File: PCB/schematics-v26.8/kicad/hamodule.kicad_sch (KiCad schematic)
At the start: 191 parts, among them J1 GND|5V, J10 Tx|Rx, J11 Sda|Scl, J12 3|9, J13 13|12, J14 3.3v|GND|7|15, J15 2604-1104, J16 2604-1104, J17 TestPoint, J19 TestPoint, J2 2604-1102, J3 USB_C_Receptacle_USB2.0, J4 GND|3.3V, J5 Conn_01x02_Pin, J6 2604-1104, J7 2604-1104, J8 5v|GND|Do, J9 Screen, K1 AQG22205, K2 AQG22205, K3 AQG22205, K4 AQG22205, K5 AQG22205, K6 AQG22205, K7 AQG22205, K8 AQG22205, SW1 USB | PS, SW2 Reset, SW3 Boot, U1 LD1117AV33, U10 SN74LV1T34DBV, U11 ULN2803A, U12 TCAL6416, U14 74AHC1G04, U2 USBLC6-2SC6, U3 ESP32-S3-WROOM-2, U4 LDA210, U5 LDA210, U6 LDA210, U7 LDA210, U8 SHT4x, U9 SN74LVCH8T245

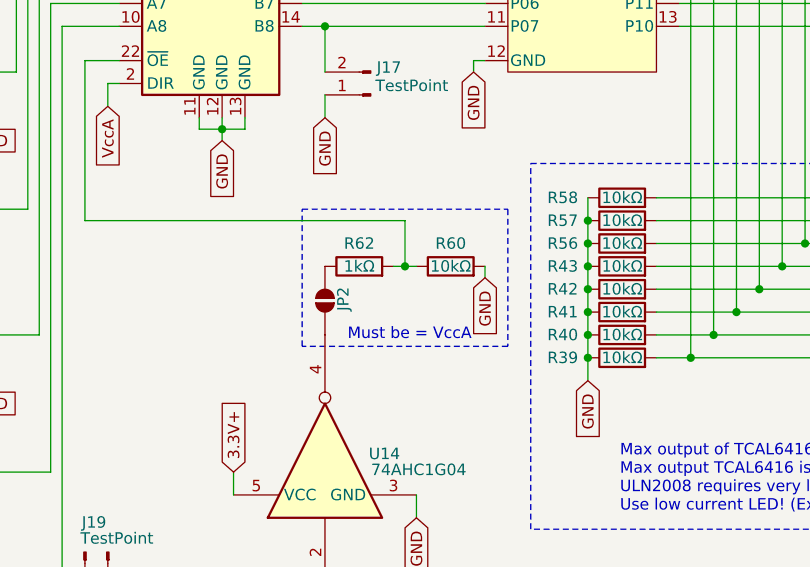
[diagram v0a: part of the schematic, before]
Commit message: areas were not properly filled in PCB
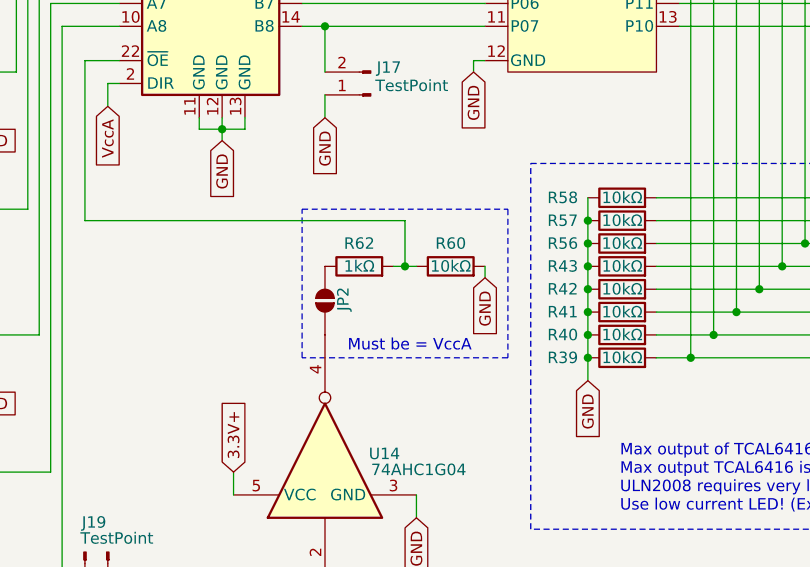
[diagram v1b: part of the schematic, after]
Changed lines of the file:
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@@
 	(rectangle
 		(start 246.38 127)
-		(end 269.24 142.24)
+		(end 269.24 143.51)
 		(stroke
 			(width 0)
@@
 	(text "Must be = VccA"
 		(exclude_from_sim no)
-		(at 258.318 140.97 0)
+		(at 258.318 142.24 0)
 		(effects
 			(font

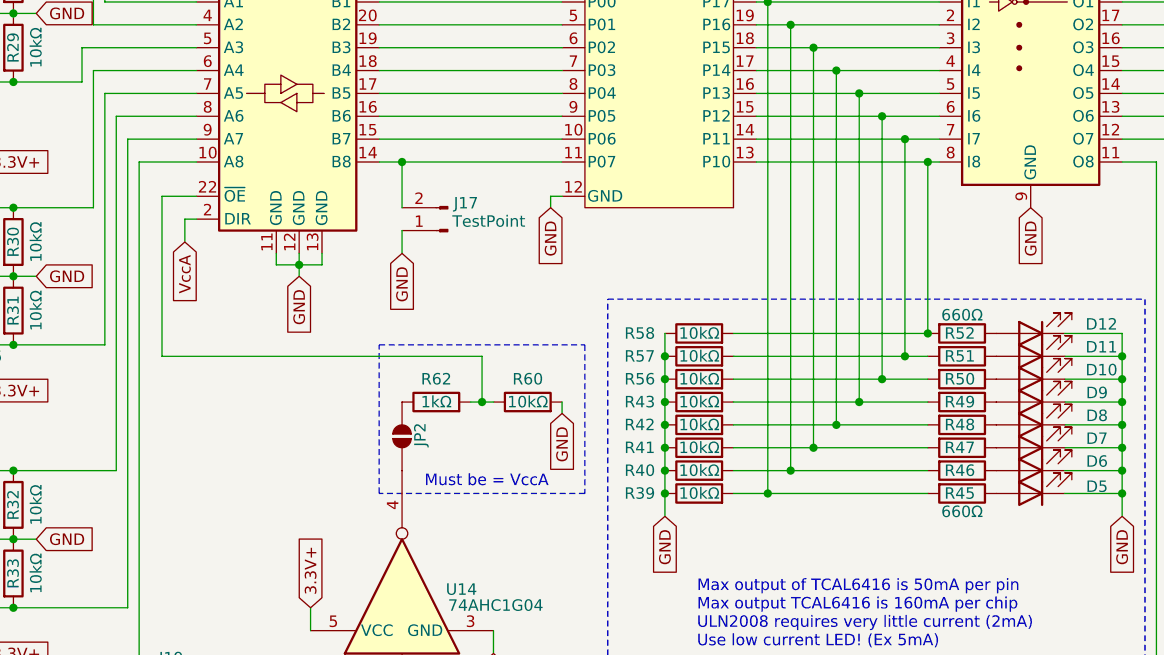
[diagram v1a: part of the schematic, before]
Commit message: Adding Test point for TCAL to ULN. Small astetic change in the schematic: Moving the voltage divider resistors after the NOT gate
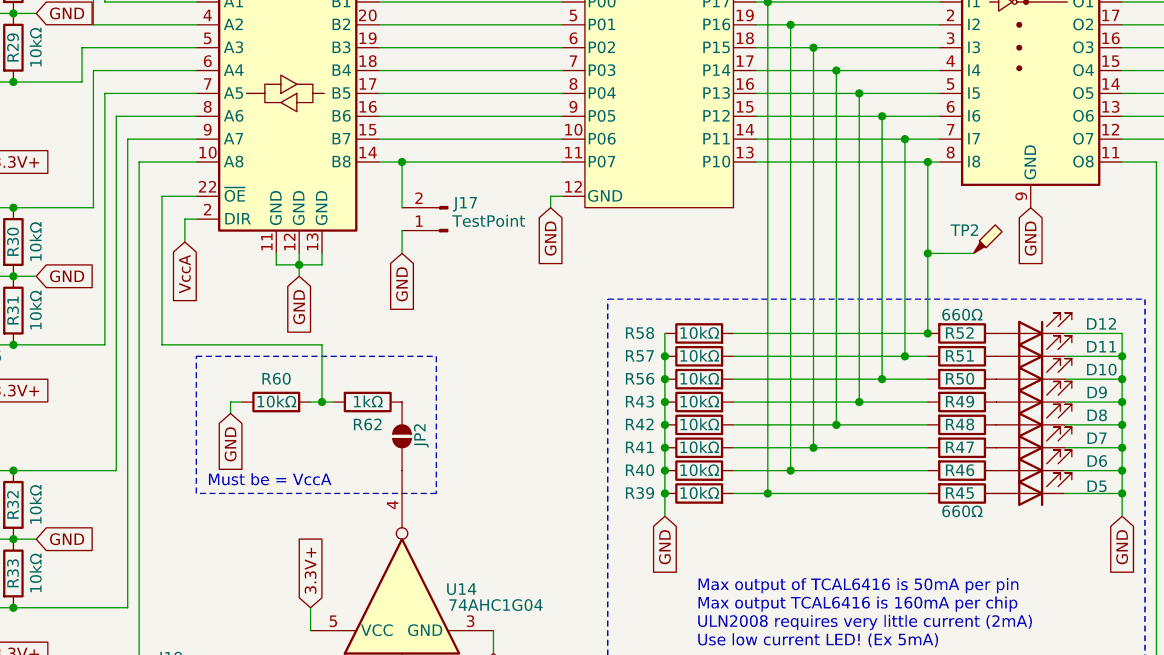
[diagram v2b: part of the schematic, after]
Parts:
- added TP2: GND, TestPoint:TestPoint_THTPad_1.0x1.0mm_Drill0.5mm, symbol Connector:TestPoint_Probe
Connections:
- net GND: now also R60.1; no longer R60.2
- net at R62.2, U9.22 (~{OE}): now also R60.2; no longer R60.1
- net at R52.2, R58.2, U11.8 (I8)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: now also TP2.1
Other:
- moved on the sheet: R60, R62
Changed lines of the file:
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@@
 	)
 	(rectangle
-		(start 246.38 127)
-		(end 269.24 143.51)
+		(start 226.06 128.27)
+		(end 252.73 143.51)
 		(stroke
 			(width 0)
@@
 	(text "Must be = VccA"
 		(exclude_from_sim no)
-		(at 258.318 142.24 0)
+		(at 234.188 142.24 0)
 		(effects
 			(font
@@
 	)
 	(junction
-		(at 257.81 133.35)
-		(diameter 0)
-		(color 0 0 0 0)
-	)
-	(junction
 		(at 95.25 77.47)
 		(diameter 0)
@@
 	)
 	(junction
+		(at 240.03 133.35)
+		(diameter 0)
+		(color 0 0 0 0)
+	)
+	(junction
 		(at 207.01 215.9)
 		(diameter 0)
@@
 	)
 	(junction
+		(at 307.34 116.84)
+		(diameter 0)
+		(color 0 0 0 0)
+	)
+	(junction
 		(at 278.13 138.43)
 		(diameter 0)
@@
 	(wire
 		(pts
+			(xy 238.76 133.35) (xy 240.03 133.35)
+		)
+		(stroke
+			(width 0)
+			(type default)
+		)
+	)
+	(wire
+		(pts
 			(xy 292.1 215.9) (xy 295.91 215.9)
 		)
@@
 	(wire
 		(pts
+			(xy 240.03 133.35) (xy 241.3 133.35)
+		)
+		(stroke
+			(width 0)
+			(type default)
+		)
+	)
+	(wire
+		(pts
 			(xy 63.5 133.35) (xy 63.5 130.81)
 		)
@@
 	(wire
 		(pts
-			(xy 257.81 133.35) (xy 259.08 133.35)
-		)
-		(stroke
-			(width 0)
-			(type default)
-		)
-	)
-	(wire
-		(pts
 			(xy 328.93 93.98) (xy 339.09 93.98)
 		)
@@
 	(wire
 		(pts
+			(xy 307.34 116.84) (xy 312.42 116.84)
+		)
+		(stroke
+			(width 0)
+			(type default)
+		)
+	)
+	(wire
+		(pts
 			(xy 382.27 113.03) (xy 368.3 113.03)
 		)
@@
 	(wire
 		(pts
+			(xy 229.87 134.62) (xy 229.87 133.35)
+		)
+		(stroke
+			(width 0)
+			(type default)
+		)
+	)
+	(wire
+		(pts
 			(xy 265.43 73.66) (xy 266.7 73.66)
 		)
@@
 	(wire
 		(pts
-			(xy 222.25 128.27) (xy 257.81 128.27)
+			(xy 222.25 127) (xy 240.03 127)
 		)
 		(stroke
@@
 	(wire
 		(pts
+			(xy 229.87 133.35) (xy 231.14 133.35)
+		)
+		(stroke
+			(width 0)
+			(type default)
+		)
+	)
+	(wire
+		(pts
 			(xy 285.75 133.35) (xy 299.72 133.35)
 		)
@@
 	(wire
 		(pts
-			(xy 266.7 133.35) (xy 266.7 134.62)
-		)
-		(stroke
-			(width 0)
-			(type default)
-		)
-	)
-	(wire
-		(pts
 			(xy 152.4 156.21) (xy 153.67 156.21)
 		)
@@
 	(wire
 		(pts
-			(xy 307.34 106.68) (xy 307.34 125.73)
+			(xy 307.34 106.68) (xy 307.34 116.84)
 		)
 		(stroke
@@
 	(wire
 		(pts
-			(xy 257.81 133.35) (xy 256.54 133.35)
-		)
-		(stroke
-			(width 0)
-			(type default)
-		)
-	)
-	(wire
-		(pts
 			(xy 41.91 59.69) (xy 45.72 59.69)
 		)
@@
 	(wire
 		(pts
-			(xy 222.25 110.49) (xy 222.25 128.27)
+			(xy 222.25 110.49) (xy 222.25 127)
 		)
 		(stroke
@@
 	(wire
 		(pts
-			(xy 257.81 128.27) (xy 257.81 133.35)
+			(xy 240.03 127) (xy 240.03 133.35)
 		)
 		(stroke
@@
 	(wire
 		(pts
+			(xy 307.34 116.84) (xy 307.34 125.73)
+		)
+		(stroke
+			(width 0)
+			(type default)
+		)
+	)
+	(wire
+		(pts
 			(xy 201.93 165.1) (xy 201.93 161.29)
 		)
@@
 	(global_label "GND"
 		(shape input)
-		(at 266.7 134.62 270)
+		(at 229.87 134.62 270)
 		(fields_autoplaced yes)
 		(effects
@@
 		)
 		(property "Intersheetrefs" "${INTERSHEET_REFS}"
-			(at 266.7 140.8215 90)
+			(at 229.87 140.8215 90)
 			(effects
 				(font
@@
 	)
 	(symbol
+		(lib_id "Connector:TestPoint_Probe")
+		(at 312.42 116.84 0)
+		(unit 1)
+		(exclude_from_sim no)
+		(in_bom yes)
+		(on_board yes)
+		(dnp no)
+		(property "Reference" "TP2"
+			(at 309.88 114.3 0)
+			(effects
+				(font
+					(size 1.27 1.27)
+				)
+				(justify left)
+			)
+		)
+		(property "Value" "GND"
+			(at 316.23 116.5224 0)
+			(effects
+				(font
+					(size 1.27 1.27)
+				)
+				(justify left)
+				(hide yes)
+			)
+		)
+		(property "Footprint" "TestPoint:TestPoint_THTPad_1.0x1.0mm_Drill0.5mm"
+			(at 317.5 116.84 0)
+			(effects
+				(font
+					(size 1.27 1.27)
+				)
+				(hide yes)
+			)
+		)
+		(property "Datasheet" "~"
+			(at 317.5 116.84 0)
+			(effects
+				(font
+					(size 1.27 1.27)
+				)
+				(hide yes)
+			)
+		)
+		(property "Description" "test point (alternative probe-style design)"
+			(at 312.42 116.84 0)
+			(effects
+				(font
+					(size 1.27 1.27)
+				)
+				(hide yes)
+			)
+		)
+		(property "Field4" ""
+			(at 312.42 116.84 0)
+			(effects
+				(font
+					(size 1.27 1.27)
+				)
+				(hide yes)
+			)
+		)
+		(pin "1"
+		)
+		(instances
+			(project "hamodule"
+				(path "/e5217a0c-7f55-4c30-adda-7f8d95709d1b"
+					(reference "TP2")
+					(unit 1)
+				)
+			)
+		)
+	)
+	(symbol
 		(lib_id "Device:C_Small")
 		(at 201.93 143.51 0)
@@
 	(symbol
 		(lib_id "Device:R")
-		(at 252.73 133.35 90)
+		(at 245.11 133.35 270)
 		(unit 1)
 		(exclude_from_sim no)
@@
 		(dnp no)
 		(property "Reference" "R62"
-			(at 252.73 130.81 90)
+			(at 245.11 135.89 90)
 			(effects
 				(font
@@
 		)
 		(property "Value" "1kΩ"
-			(at 252.73 133.35 90)
+			(at 245.11 133.35 90)
 			(effects
 				(font
@@
 		)
 		(property "Footprint" "Resistor_SMD:R_0603_1608Metric_Pad0.98x0.95mm_HandSolder"
-			(at 252.73 135.128 90)
+			(at 245.11 131.572 90)
 			(effects
 				(font
@@
 		)
 		(property "Datasheet" "~"
-			(at 252.73 133.35 0)
+			(at 245.11 133.35 0)
 			(effects
 				(font
@@
 		)
 		(property "Description" "Resistor"
-			(at 252.73 133.35 0)
+			(at 245.11 133.35 0)
 			(effects
 				(font
@@
 		)
 		(property "JLCPCB" "C21190"
-			(at 252.73 133.35 90)
+			(at 245.11 133.35 90)
 			(effects
 				(font
@@
 		)
 		(property "LCSC" "C21190"
-			(at 252.73 133.35 0)
+			(at 245.11 133.35 0)
 			(effects
 				(font
@@
 		)
 		(property "Field4" ""
-			(at 252.73 133.35 0)
+			(at 245.11 133.35 0)
 			(effects
 				(font
@@
 		)
 		(property "PcbText" ""
-			(at 252.73 133.35 0)
+			(at 245.11 133.35 0)
 			(effects
 				(font
@@
 	(symbol
 		(lib_id "Device:R")
-		(at 262.89 133.35 90)
+		(at 234.95 133.35 90)
 		(unit 1)
 		(exclude_from_sim no)
@@
 		(dnp no)
 		(property "Reference" "R60"
-			(at 262.89 130.81 90)
+			(at 234.95 130.81 90)
 			(effects
 				(font
@@
 		)
 		(property "Value" "10kΩ"
-			(at 262.89 133.35 90)
+			(at 234.95 133.35 90)
 			(effects
 				(font
@@
 		)
 		(property "Footprint" "Resistor_SMD:R_0603_1608Metric_Pad0.98x0.95mm_HandSolder"
-			(at 262.89 135.128 90)
+			(at 234.95 135.128 90)
 			(effects
 				(font
@@
 		)
 		(property "Datasheet" "~"
-			(at 262.89 133.35 0)
+			(at 234.95 133.35 0)
 			(effects
 				(font
@@
 		)
 		(property "Description" "Resistor"
-			(at 262.89 133.35 0)
+			(at 234.95 133.35 0)
 			(effects
 				(font
@@
 		)
 		(property "JLCPCB" "C25804"
-			(at 262.89 133.35 90)
+			(at 234.95 133.35 90)
 			(effects
 				(font
@@
 		)
 		(property "LCSC" "C25804"
-			(at 262.89 133.35 0)
+			(at 234.95 133.35 0)
 			(effects
 				(font
@@
 		)
 		(property "Field4" ""
-			(at 262.89 133.35 0)
+			(at 234.95 133.35 0)
 			(effects
 				(font

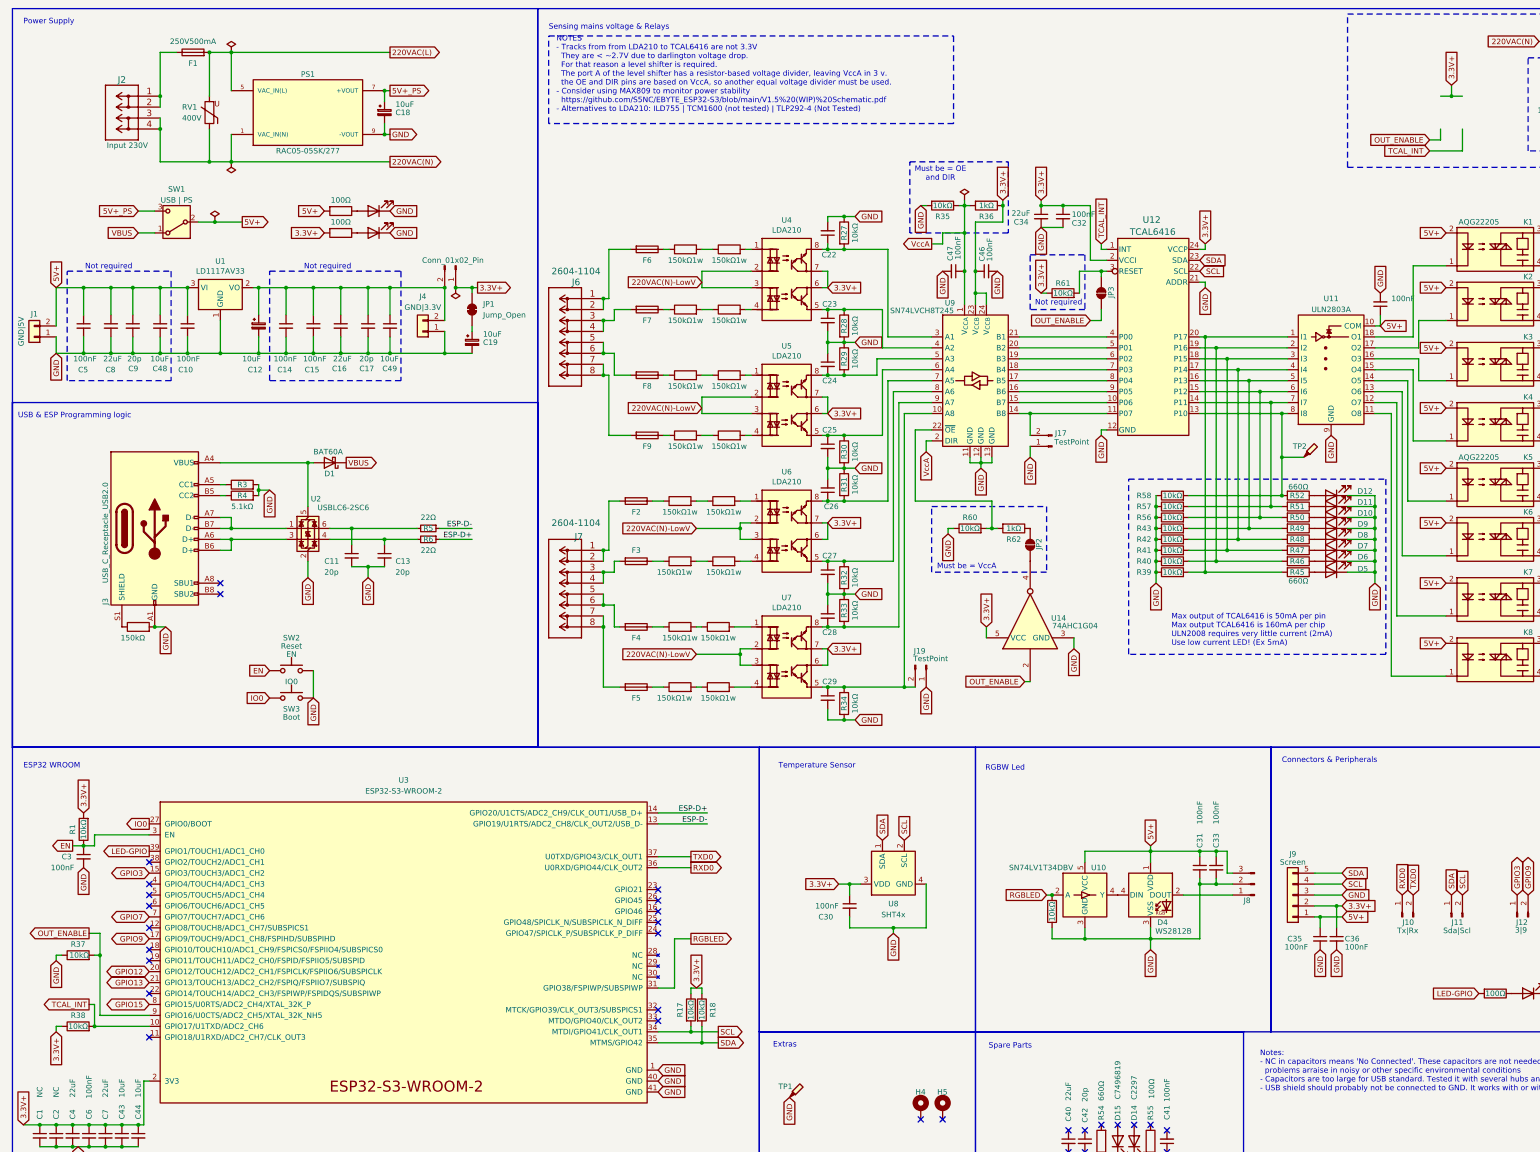
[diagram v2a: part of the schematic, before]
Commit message: [V26] Rearranging some nets. Fixing some connections that were missing. Solving some ERC. Updating UL28003 footprint to match current library
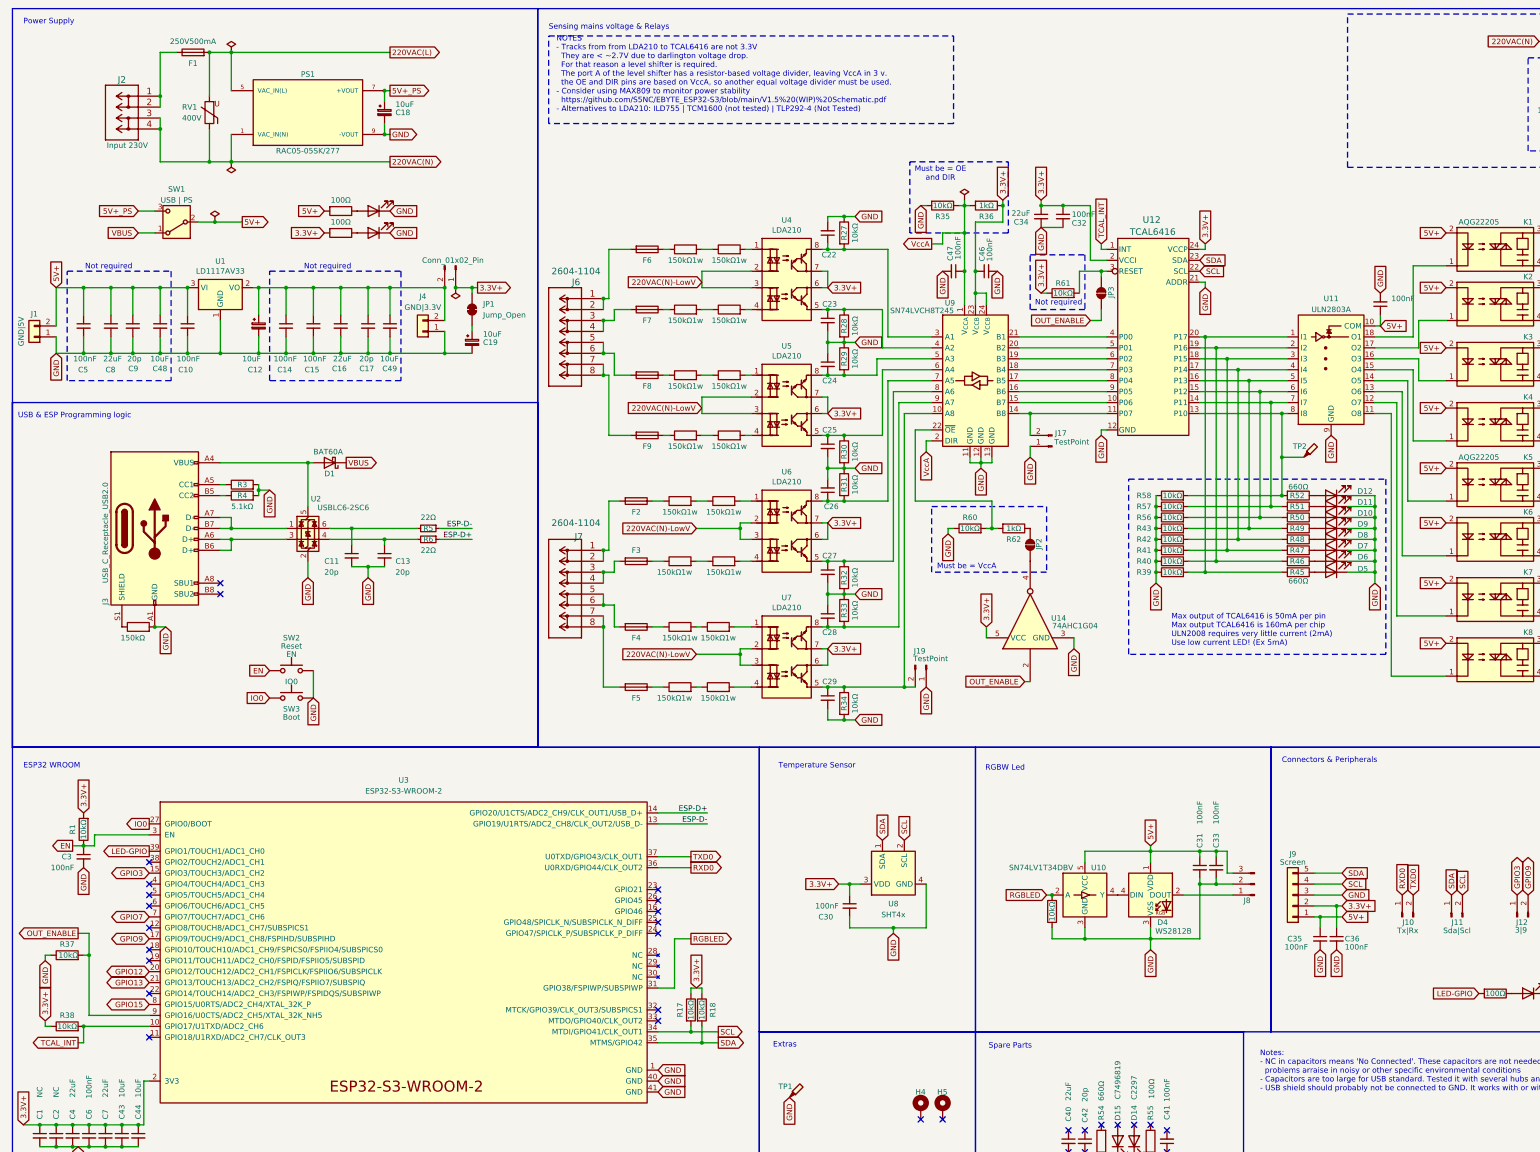
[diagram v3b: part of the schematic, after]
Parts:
- K1, K2, K3, K4, K5, K6, K7, K8: footprint AQG12205:AQG12205 -> AQG12205
- PS1: footprint rac05-05sk:277 -> CONV_RAC05-05SK/277
- U1: footprint Package_TO_SOT_THT:TO-220-3_Vertical -> Package_TO_SOT_SMD:SOT-223-3_TabPin2
- U11: footprint Package_SO:SOP-18_7x12.5mm_P1.27mm -> Package_SO:SOIC-18W_7.5x11.6mm_P1.27mm
- U8: footprint sht40:XDCR_SHT40-AD1B-R2 -> Sensor:SHT4x
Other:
- moved on the sheet: R37, R38
